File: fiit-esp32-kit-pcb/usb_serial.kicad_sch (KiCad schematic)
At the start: 30 parts, among them J8 USB_C_Receptacle_USB2.0, J9 USB_C_Receptacle_USB2.0, Q1 MMDT3904, U3 CP2102N-Axx-xQFN28

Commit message: footprints assignment
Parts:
- JP4: renamed from JP3; footprint (none) -> Jumper:SolderJumper-2_P1.3mm_Bridged_RoundedPad1.0x1.5mm
- JP5: renamed from JP4; footprint (none) -> Jumper:SolderJumper-2_P1.3mm_Bridged_RoundedPad1.0x1.5mm
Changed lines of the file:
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@@
 		(dnp no)
 		(fields_autoplaced yes)
-		(property "Reference" "JP4"
+		(property "Reference" "JP5"
 			(at 100.33 121.92 0)
 			(effects
@@
 			)
 		)
-		(property "Footprint" ""
+		(property "Footprint" "Jumper:SolderJumper-2_P1.3mm_Bridged_RoundedPad1.0x1.5mm"
 			(at 100.33 128.27 0)
 			(effects
@@
 			(project "fiit-esp32-kit-pcb"
 				(path "/d7013812-ce13-4db9-a6cc-42acdc5acaf9/7a988d19-92b6-49d4-ae77-db839e758892"
-					(reference "JP4")
+					(reference "JP5")
 					(unit 1)
 				)
@@
 		(dnp no)
 		(fields_autoplaced yes)
-		(property "Reference" "JP3"
+		(property "Reference" "JP4"
 			(at 100.33 52.07 0)
 			(effects
@@
 			)
 		)
-		(property "Footprint" ""
+		(property "Footprint" "Jumper:SolderJumper-2_P1.3mm_Bridged_RoundedPad1.0x1.5mm"
 			(at 100.33 58.42 0)
 			(effects
@@
 			(project ""
 				(path "/d7013812-ce13-4db9-a6cc-42acdc5acaf9/7a988d19-92b6-49d4-ae77-db839e758892"
-					(reference "JP3")
+					(reference "JP4")
 					(unit 1)
 				)

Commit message: updated manufacturer part numbers
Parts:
- R12: LCSC (none) -> C25961; Manufacturer Part Number (none) -> 0603WAF2212T5E
- R13: LCSC (none) -> C23061; Manufacturer Part Number (none) -> 0603WAF4752T5E
- U3: LCSC (none) -> C964632; Manufacturer Part Number (none) -> CP2102N-A02-GQFN28R
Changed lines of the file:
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@@
 			)
 		)
+		(property "LCSC" "~"
+			(at 100.33 128.27 0)
+			(effects
+				(font
+					(size 1.27 1.27)
+				)
+			)
+		)
+		(property "Manufacturer Part Number" "~"
+			(at 100.33 128.27 0)
+			(effects
+				(font
+					(size 1.27 1.27)
+				)
+			)
+		)
 		(pin "1"
 		)
@@
 			)
 		)
+		(property "LCSC" "~"
+			(at 100.33 58.42 0)
+			(effects
+				(font
+					(size 1.27 1.27)
+				)
+			)
+		)
+		(property "Manufacturer Part Number" "~"
+			(at 100.33 58.42 0)
+			(effects
+				(font
+					(size 1.27 1.27)
+				)
+			)
+		)
 		(pin "1"
 		)
@@
 			)
 		)
-		(property "LCSC" ""
+		(property "LCSC" "C25961"
 			(at 195.58 68.58 0)
 			(effects
@@
 			)
 		)
-		(property "Manufacturer Part Number" ""
+		(property "Manufacturer Part Number" "0603WAF2212T5E"
 			(at 195.58 68.58 0)
 			(effects
@@
 			)
 		)
+		(property "LCSC" "C964632"
+			(at 237.49 83.82 0)
+			(effects
+				(font
+					(size 1.27 1.27)
+				)
+				(hide yes)
+			)
+		)
+		(property "Manufacturer Part Number" "CP2102N-A02-GQFN28R"
+			(at 237.49 83.82 0)
+			(effects
+				(font
+					(size 1.27 1.27)
+				)
+				(hide yes)
+			)
+		)
 		(pin "29"
 		)
@@
 			)
 		)
-		(property "LCSC" ""
+		(property "LCSC" "C23061"
 			(at 200.66 73.66 0)
 			(effects
@@
 			)
 		)
-		(property "Manufacturer Part Number" ""
+		(property "Manufacturer Part Number" "0603WAF4752T5E"
 			(at 200.66 73.66 0)
 			(effects

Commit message: component placement
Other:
- company: STU FIIT -> FIIT STU
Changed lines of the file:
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@@
 	(title_block
 		(title "FIIT ESP32 Kit")
-		(date "2024-07-17")
+		(date "2024-07-21")
 		(rev "0.1")
-		(company "STU FIIT")
+		(company "FIIT STU")
 		(comment 1 "Ing. Matej Pončák")
 	)

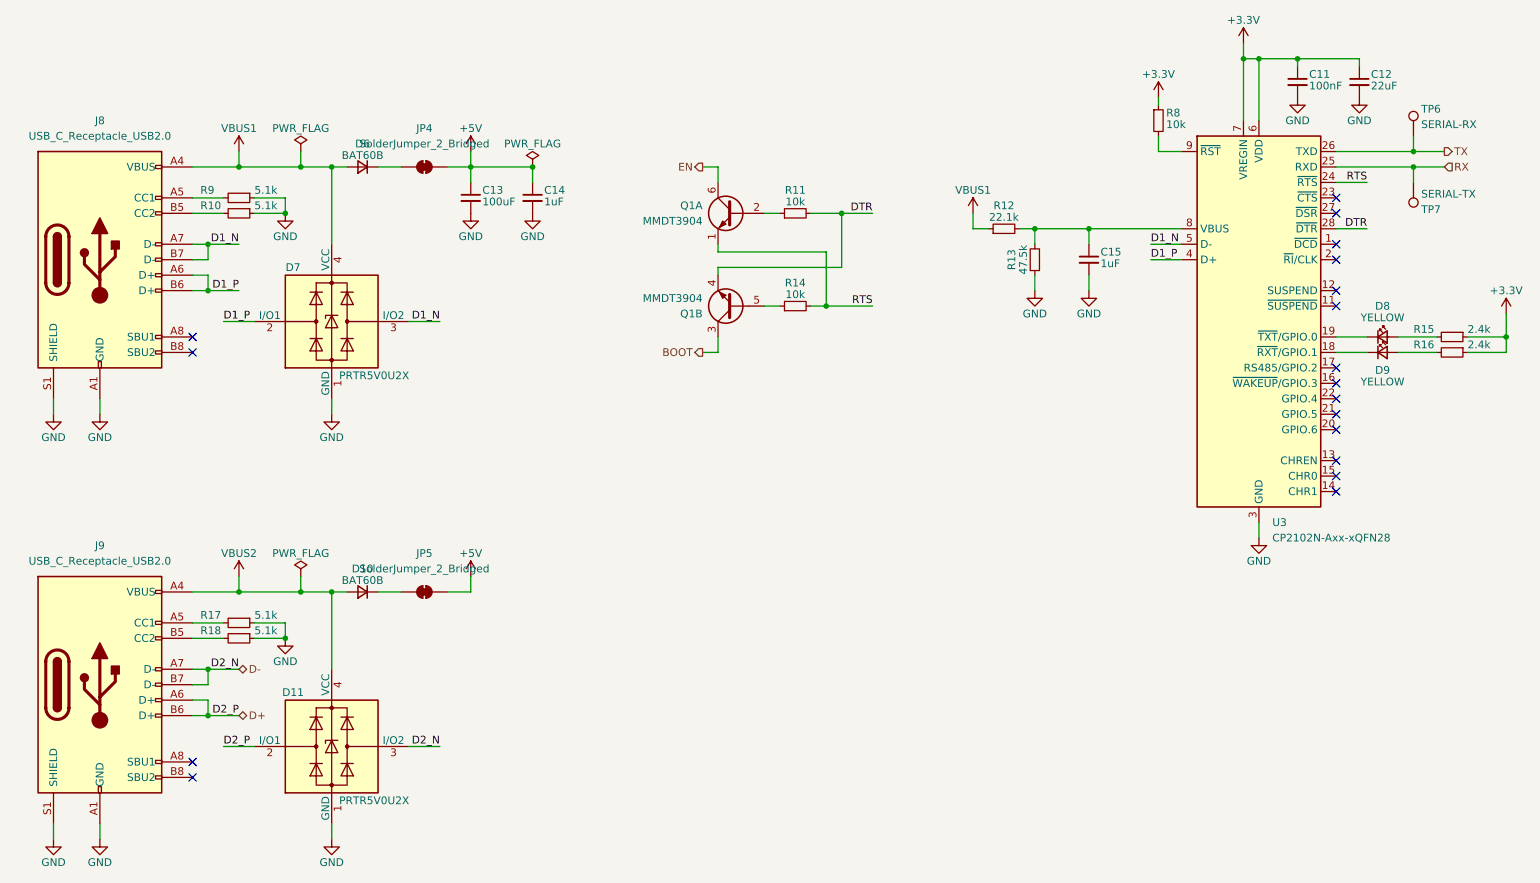
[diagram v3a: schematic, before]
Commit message: updated components placement (unrouted 237)
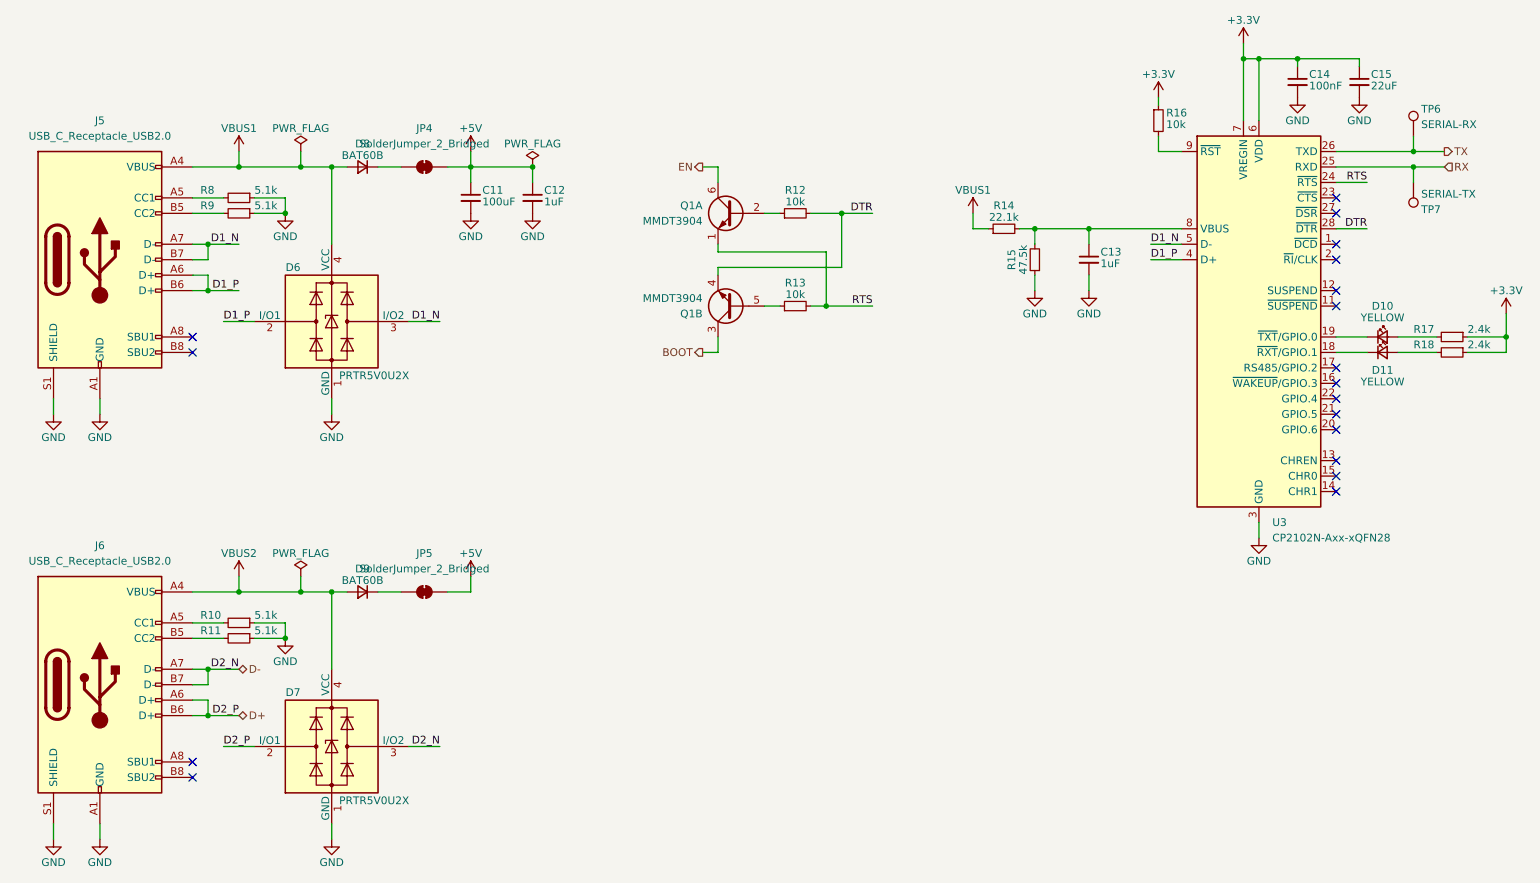
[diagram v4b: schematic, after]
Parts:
- renumbered C13 to C11, C14 to C12, C15 to C13, C11 to C14, C12 to C15, D8 to D10, D9 to D11, D7 to D6, D11 to D7, D6 to D8, D10 to D9, J8 to J5, J9 to J6, R17 to R10, R18 to R11, R11 to R12, R14 to R13, R12 to R14, R13 to R15, R8 to R16, R15 to R17, R16 to R18, R9 to R8, R10 to R9
